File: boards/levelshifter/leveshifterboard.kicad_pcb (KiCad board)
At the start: 2 copper layers, 82.5 x 43.2 mm, 40 parts, among them J1 RJ45, P1 CONN_2, P2 CONN_7, Q1 IRLR110, Q2 NDS355, SW1 SW_PUSH, U1 LM358, U2 SN74LVC1G74, U3 74HCT125, U4 TS2937

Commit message: Fixed levelshifter board
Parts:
- removed Q1: IRLR110, DPAK2
- added D5: ZENER_5.6V, sod123, F.Cu at (158.8, 61.6)
- added D6: ZENER_5.6V, sod123, F.Cu at (148.6, 60.3)
- added D7: ZENER_5.6V, sod123, F.Cu at (144.1, 75.6)
- added D8: ZENER_5.6V, sod123, F.Cu at (146.7, 75.6)
- added R13: 1k, SM0603, F.Cu at (144.8, 63.5)
- added R14: 1k, SM0603, F.Cu at (144.8, 66.0)
- added R15: 1k, SM0603, F.Cu at (144.8, 68.6)
- added R16: 1k, SM0603, F.Cu at (144.8, 71.1)
- added U5: BTS462, TO252-5L, F.Cu at (189.2, 81.3)
- C1: value 100n -> 100nF
- C2, C7: value 100nf -> 100nF
- F1: footprint fuse1 -> fuse22.5
- U2: value SN74LVC1G74 -> 74HC74; footprint SO8E -> SO14E
- moved P1 29.8 mm to (168.3, 48.3)
- moved C7 13.1 mm to (173.4, 62.9), turned to 90 degrees
- moved F1 6.75 mm to (139.7, 51.4)
- moved U2 2.54 mm to (177.2, 67.9), turned to 0 degrees
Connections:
- J1 pad 10: Sense -> (no net)
- R8 pad 1: N-0000024 -> N-0000010
- SW1 pad 1: N-0000024 -> N-0000010
- U2 pad 1: GND -> N-0000010
- U2 pad 3: PowerOn -> GND
- U2 pad 4: GND -> Shutdown
- U2 pad 6: N-0000024 -> PowerOn
- U2 pad 7: Shutdown -> GND
- U2 pad 8: +5V -> (no net)
- U3 pad 11: Reset -> N-0000015
- U3 pad 3: Clock -> N-0000018
- U3 pad 6: Enable -> N-0000017
- U3 pad 8: Data_Out -> N-0000016
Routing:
- net N-0000029: track 7.62 -> 40.4 mm
- net N-0000024: track 26.8 -> 0.00 mm, vias 1 -> 0
- net N-0000010: track 0.00 -> 25.2 mm, vias 0 -> 1
- net N-0000016: track 0.00 -> 15.8 mm, vias 0 -> 3
- net Clock: track 23.8 -> 8.13 mm
- net N-0000018: track 0.00 -> 15.6 mm
- net N-0000015: track 0.00 -> 14.2 mm, vias 0 -> 2
- net N-0000017: track 0.00 -> 13.6 mm, vias 0 -> 2
- net Reset: track 20.5 -> 8.13 mm
- net PowerOn: track 26.2 -> 14.8 mm
- net Data_Out: track 19.1 -> 8.38 mm, vias 3 -> 1
- net Enable: track 18.6 -> 8.13 mm
- net +5V: track 86.6 -> 93.1 mm, vias 5 -> 3
- net Shutdown: track 16.8 -> 18.2 mm
- net N-0000031: track 65.2 -> 64.1 mm

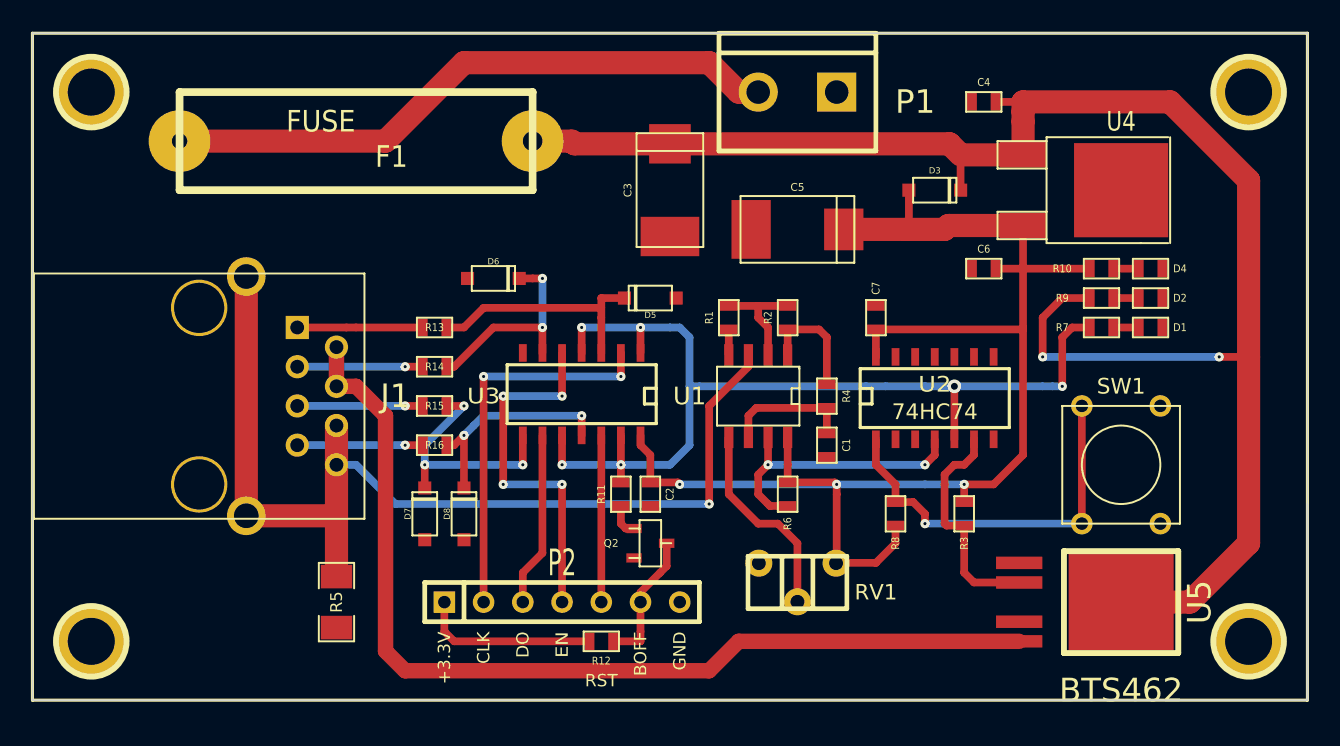
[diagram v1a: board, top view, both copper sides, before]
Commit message: Minor Silkscreen fixes
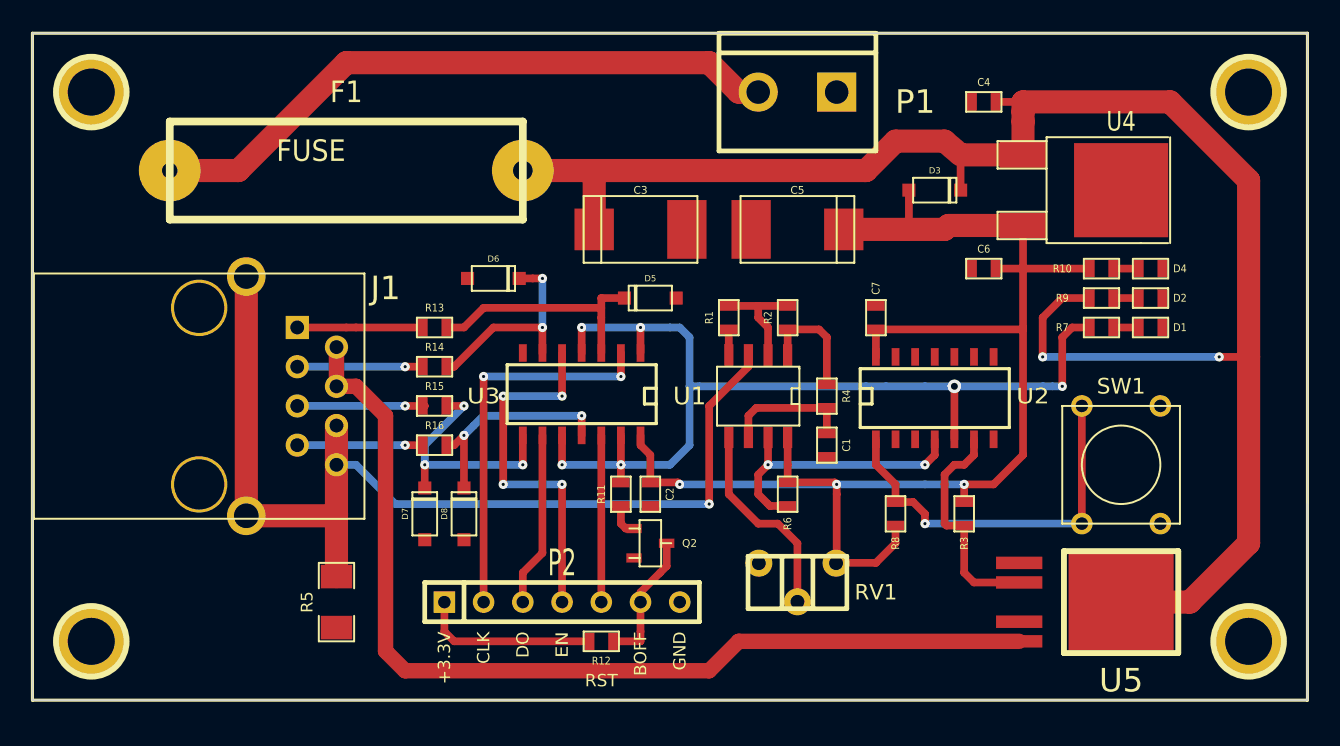
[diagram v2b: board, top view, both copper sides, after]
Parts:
- moved C3 3.18 mm to (158.1, 57.1), turned to 180 degrees
- moved F1 2.01 mm to (139.1, 53.3)
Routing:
- net +24V: track 109.7 -> 114.9 mm
- net N-0000029: track 40.4 -> 41.8 mm
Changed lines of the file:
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@@
     (thickness 1.6)
     (drawings 31)
-    (tracks 260)
+    (tracks 262)
     (zones 0)
     (modules 48)
@@
   (layers
     (15 F.Cu signal)
-    (0 B.Cu signal)
+    (0 B.Cu signal hide)
     (16 B.Adhes user)
     (17 F.Adhes user)
@@
     (descr SOT23)
     (attr smd)
-    (fp_text reference Q2 (at 0 2.54 360) (layer F.SilkS)
+    (fp_text reference Q2 (at 0 -2.54 360) (layer F.SilkS)
       (effects (font (size 0.50038 0.50038) (thickness 0.09906)))
     )
@@
     (at 138.43 81.28 270)
     (attr smd)
-    (fp_text reference R5 (at 0 0 270) (layer F.SilkS)
+    (fp_text reference R5 (at 0 1.905 270) (layer F.SilkS)
       (effects (font (size 0.762 0.762) (thickness 0.127)))
     )
@@
     (at 129.54 67.945 270)
     (tags RJ45)
-    (fp_text reference J1 (at 0 -12.7 360) (layer F.SilkS)
+    (fp_text reference J1 (at -6.985 -12.065 360) (layer F.SilkS)
       (effects (font (size 1.524 1.524) (thickness 0.3048)))
     )
@@
     (at 168.275 57.15)
     (descr "SMT capacitor, tantalum size D")
-    (fp_text reference C5 (at 0 -2.7305) (layer F.SilkS)
+    (fp_text reference C5 (at 0 -2.54) (layer F.SilkS)
       (effects (font (size 0.50038 0.50038) (thickness 0.11938)))
     )
@@
   )
   (module c_tant_D (layer F.Cu)
-    (at 160.02 54.61 90)
+    (at 158.115 57.15 180)
     (descr "SMT capacitor, tantalum size D")
-    (fp_text reference C3 (at 0 -2.7305 90) (layer F.SilkS)
+    (fp_text reference C3 (at 0 2.54 180) (layer F.SilkS)
       (effects (font (size 0.50038 0.50038) (thickness 0.11938)))
     )
-    (fp_text value 10uF (at 0 2.7305 90) (layer F.SilkS) hide
+    (fp_text value 10uF (at 0 2.7305 180) (layer F.SilkS) hide
       (effects (font (size 0.50038 0.50038) (thickness 0.11938)))
     )
@@
     (fp_line (start 3.683 2.159) (end 3.683 -2.159) (layer F.SilkS) (width 0.127))
     (fp_line (start 3.683 -2.159) (end -3.683 -2.159) (layer F.SilkS) (width 0.127))
-    (pad 1 smd rect (at 2.99974 0 90) (size 2.55016 2.70002)
+    (pad 1 smd rect (at 2.99974 0 180) (size 2.55016 2.70002)
       (layers F.Cu F.Paste F.Mask)
       (net 1 +24V)
     )
-    (pad 2 smd rect (at -2.99974 0 90) (size 2.55016 3.79984)
+    (pad 2 smd rect (at -2.99974 0 180) (size 2.55016 3.79984)
       (layers F.Cu F.Paste F.Mask)
       (net 12 GND)
@@
     (at 158.75 61.595 180)
     (descr SOD123)
-    (fp_text reference D5 (at 0 -1.09982 180) (layer F.SilkS)
+    (fp_text reference D5 (at 0 1.27 180) (layer F.SilkS)
       (effects (font (size 0.39878 0.39878) (thickness 0.09906)))
     )
@@
     (at 148.59 60.325)
     (descr SOD123)
-    (fp_text reference D6 (at 0 -1.09982) (layer F.SilkS)
+    (fp_text reference D6 (at 0 -1.27) (layer F.SilkS)
       (effects (font (size 0.39878 0.39878) (thickness 0.09906)))
     )
@@
     (at 144.145 75.565 90)
     (descr SOD123)
-    (fp_text reference D7 (at 0 -1.09982 90) (layer F.SilkS)
+    (fp_text reference D7 (at 0 -1.27 90) (layer F.SilkS)
       (effects (font (size 0.39878 0.39878) (thickness 0.09906)))
     )
@@
     (at 146.685 75.565 90)
     (descr SOD123)
-    (fp_text reference D8 (at 0 -1.09982 90) (layer F.SilkS)
+    (fp_text reference D8 (at 0 -1.27 90) (layer F.SilkS)
       (effects (font (size 0.39878 0.39878) (thickness 0.09906)))
     )
@@
     (at 144.78 63.5 180)
     (attr smd)
-    (fp_text reference R13 (at 0 0 180) (layer F.SilkS)
+    (fp_text reference R13 (at 0 1.27 180) (layer F.SilkS)
       (effects (font (size 0.508 0.4572) (thickness 0.1143)))
     )
@@
     (at 144.78 66.04 180)
     (attr smd)
-    (fp_text reference R14 (at 0 0 180) (layer F.SilkS)
+    (fp_text reference R14 (at 0 1.27 180) (layer F.SilkS)
       (effects (font (size 0.508 0.4572) (thickness 0.1143)))
     )
@@
     (at 144.78 68.58 180)
     (attr smd)
-    (fp_text reference R15 (at 0 0 180) (layer F.SilkS)
+    (fp_text reference R15 (at 0 1.27 180) (layer F.SilkS)
       (effects (font (size 0.508 0.4572) (thickness 0.1143)))
     )
@@
     (at 144.78 71.12 180)
     (attr smd)
-    (fp_text reference R16 (at 0 0 180) (layer F.SilkS)
+    (fp_text reference R16 (at 0 1.27 180) (layer F.SilkS)
       (effects (font (size 0.508 0.4572) (thickness 0.1143)))
     )
@@
     (tags "CMS SOJ")
     (attr smd)
-    (fp_text reference U2 (at 0 -0.762) (layer F.SilkS)
+    (fp_text reference U2 (at 6.35 0) (layer F.SilkS)
       (effects (font (size 1.016 1.143) (thickness 0.127)))
     )
-    (fp_text value 74HC74 (at 0 1.016) (layer F.SilkS)
+    (fp_text value 74HC74 (at 0 1.016) (layer F.SilkS) hide
       (effects (font (size 1.016 1.016) (thickness 0.127)))
     )
@@
   (module TO252-5L (layer F.Cu)
     (at 189.23 81.28 270)
-    (fp_text reference U5 (at 0 -5.08 270) (layer F.SilkS)
+    (fp_text reference U5 (at 5.08 0 360) (layer F.SilkS)
       (effects (font (size 1.524 1.524) (thickness 0.3048)))
     )
-    (fp_text value BTS462 (at 5.715 0 360) (layer F.SilkS)
+    (fp_text value BTS462 (at 5.08 0 360) (layer F.SilkS) hide
       (effects (font (size 1.524 1.524) (thickness 0.3048)))
     )
@@
   )
   (module fuse22.5 (layer F.Cu)
-    (at 139.7 51.435)
+    (at 139.065 53.34)
     (descr "Resitance 7 pas")
     (tags R)
     (autoplace_cost180 10)
-    (fp_text reference F1 (at 2.286 1.016) (layer F.SilkS)
+    (fp_text reference F1 (at 0 -5.08) (layer F.SilkS)
       (effects (font (size 1.397 1.27) (thickness 0.2032)))
     )
@@
     (arrow2b (pts (xy 102.87 40.005001) (xy 103.996503 39.418581)))
   )
-  (segment (start 160.02 51.61026) (end 153.84526 51.61026) (width 1.5) (layer F.Cu) (net 1))
-  (segment (start 153.67 51.435) (end 151.13 51.435) (width 1.5) (layer F.Cu) (net 1))
-  (segment (start 153.84526 51.61026) (end 153.67 51.435) (width 1.5) (layer F.Cu) (net 1))
+  (segment (start 155.11526 57.15) (end 155.11526 53.34) (width 1.5) (layer F.Cu) (net 1) (status 400000))
+  (segment (start 172.72 53.34) (end 155.575 53.34) (width 1.5) (layer F.Cu) (net 1))
+  (segment (start 155.575 53.34) (end 151.13 53.34) (width 1.5) (layer F.Cu) (net 1))
+  (segment (start 174.625 51.435) (end 172.72 53.34) (width 1.5) (layer F.Cu) (net 1))
+  (segment (start 178.83886 52.324) (end 177.8 51.435) (width 1.5) (layer F.Cu) (net 1))
+  (segment (start 177.8 51.435) (end 174.625 51.435) (width 1.5) (layer F.Cu) (net 1))
+  (segment (start 151.13 53.34) (end 150.495 53.34) (width 1.5) (layer F.Cu) (net 1) (status 800020))
   (segment (start 181.102 48.895) (end 182.88 48.895) (width 0.5) (layer F.Cu) (net 1))
   (via (at 184.15 65.405) (size 0.6) (drill 0.2) (layers F.Cu B.Cu) (net 1))
@@
   (segment (start 182.88 50.165) (end 182.88 52.324) (width 1.5) (layer F.Cu) (net 1))
   (segment (start 192.405 48.895) (end 182.88 48.895) (width 1.5) (layer F.Cu) (net 1))
-  (segment (start 178.83886 52.324) (end 178.12512 51.61026) (width 1.5) (layer F.Cu) (net 1))
-  (segment (start 178.12512 51.61026) (end 160.02 51.61026) (width 1.5) (layer F.Cu) (net 1))
   (segment (start 178.83886 54.61) (end 178.83886 52.324) (width 0.5) (layer F.Cu) (net 1))
   (segment (start 179.07 52.705) (end 179.07 52.324) (width 0.5) (layer F.Cu) (net 1))
@@
   (segment (start 169.672 63.627) (end 170.18 64.135) (width 0.5) (layer F.Cu) (net 21))
   (segment (start 167.64 65.278) (end 167.64 63.627) (width 0.5) (layer F.Cu) (net 21))
-  (segment (start 128.27 51.435) (end 141.605 51.435) (width 1.5) (layer F.Cu) (net 22))
+  (segment (start 127.635 53.34) (end 132.08 53.34) (width 1.5) (layer F.Cu) (net 22) (status 400010))
   (segment (start 164.465 48.26) (end 165.735 48.26) (width 1.5) (layer F.Cu) (net 22) (status 20))
   (segment (start 162.56 46.355) (end 164.465 48.26) (width 1.5) (layer F.Cu) (net 22))
-  (segment (start 146.685 46.355) (end 162.56 46.355) (width 1.5) (layer F.Cu) (net 22))
-  (segment (start 141.605 51.435) (end 146.685 46.355) (width 1.5) (layer F.Cu) (net 22))
+  (segment (start 139.065 46.355) (end 162.56 46.355) (width 1.5) (layer F.Cu) (net 22))
+  (segment (start 132.08 53.34) (end 139.065 46.355) (width 1.5) (layer F.Cu) (net 22))
   (segment (start 188.722 59.69) (end 190.373 59.69) (width 0.5) (layer F.Cu) (net 23) (status 10))
   (segment (start 138.43 67.31) (end 138.43 64.77) (width 1) (layer F.Cu) (net 24))

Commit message: Final fixes to board layouts
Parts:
- moved P1 5.08 mm to (163.2, 48.3)
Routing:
- net N-0000029: track 41.8 -> 35.1 mm
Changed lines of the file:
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@@
     (links 97)
     (no_connects 0)
-    (area 83.440001 10.1575 233.0475 88.1634)
+    (area 83.440001 10.1575 233.0475 87.730001)
     (thickness 1.6)
     (drawings 31)
@@
   (layers
     (15 F.Cu signal)
-    (0 B.Cu signal hide)
+    (0 B.Cu signal)
     (16 B.Adhes user)
     (17 F.Adhes user)
     (18 B.Paste user)
     (19 F.Paste user)
-    (20 B.SilkS user hide)
+    (20 B.SilkS user)
     (21 F.SilkS user)
     (22 B.Mask user)
@@
   )
   (setup
-    (last_trace_width 1.5)
+    (last_trace_width 0.254)
     (user_trace_width 0.3)
     (user_trace_width 0.5)
@@
     (visible_elements FFFFFFBF)
     (pcbplotparams
-      (layerselection 272400385)
+      (layerselection 284983297)
       (usegerberextensions true)
       (excludeedgelayer true)
@@
       (plotinvisibletext false)
       (padsonsilk false)
-      (subtractmaskfromsilk true)
+      (subtractmaskfromsilk false)
       (outputformat 1)
       (mirror false)
@@
   )
   (module bornier2 (layer F.Cu)
-    (at 168.275 48.26 180)
+    (at 163.195 48.26 180)
     (descr "Bornier d'alimentation 2 pins")
     (tags DEV)
@@
     (arrow2b (pts (xy 102.87 40.005001) (xy 103.996503 39.418581)))
   )
-  (segment (start 155.11526 57.15) (end 155.11526 53.34) (width 1.5) (layer F.Cu) (net 1) (status 400000))
+  (segment (start 155.11526 57.15) (end 155.11526 53.34) (width 1.5) (layer F.Cu) (net 1))
   (segment (start 172.72 53.34) (end 155.575 53.34) (width 1.5) (layer F.Cu) (net 1))
   (segment (start 155.575 53.34) (end 151.13 53.34) (width 1.5) (layer F.Cu) (net 1))
@@
   (segment (start 178.83886 52.324) (end 177.8 51.435) (width 1.5) (layer F.Cu) (net 1))
   (segment (start 177.8 51.435) (end 174.625 51.435) (width 1.5) (layer F.Cu) (net 1))
-  (segment (start 151.13 53.34) (end 150.495 53.34) (width 1.5) (layer F.Cu) (net 1) (status 800020))
+  (segment (start 151.13 53.34) (end 150.495 53.34) (width 1.5) (layer F.Cu) (net 1) (status 20))
   (segment (start 181.102 48.895) (end 182.88 48.895) (width 0.5) (layer F.Cu) (net 1))
   (via (at 184.15 65.405) (size 0.6) (drill 0.2) (layers F.Cu B.Cu) (net 1))
@@
   (segment (start 169.672 63.627) (end 170.18 64.135) (width 0.5) (layer F.Cu) (net 21))
   (segment (start 167.64 65.278) (end 167.64 63.627) (width 0.5) (layer F.Cu) (net 21))
-  (segment (start 127.635 53.34) (end 132.08 53.34) (width 1.5) (layer F.Cu) (net 22) (status 400010))
-  (segment (start 164.465 48.26) (end 165.735 48.26) (width 1.5) (layer F.Cu) (net 22) (status 20))
-  (segment (start 162.56 46.355) (end 164.465 48.26) (width 1.5) (layer F.Cu) (net 22))
-  (segment (start 139.065 46.355) (end 162.56 46.355) (width 1.5) (layer F.Cu) (net 22))
-  (segment (start 132.08 53.34) (end 139.065 46.355) (width 1.5) (layer F.Cu) (net 22))
+  (segment (start 137.16 48.26) (end 158.115 48.26) (width 1.5) (layer F.Cu) (net 22))
+  (segment (start 132.08 53.34) (end 137.16 48.26) (width 1.5) (layer F.Cu) (net 22))
+  (segment (start 127.635 53.34) (end 132.08 53.34) (width 1.5) (layer F.Cu) (net 22) (status 10))
+  (segment (start 158.115 48.26) (end 160.655 48.26) (width 1.5) (layer F.Cu) (net 22))
+  (segment (start 158.115 48.26) (end 158.115 48.26) (width 1.5) (layer F.Cu) (net 22))
   (segment (start 188.722 59.69) (end 190.373 59.69) (width 0.5) (layer F.Cu) (net 23) (status 10))
   (segment (start 138.43 67.31) (end 138.43 64.77) (width 1) (layer F.Cu) (net 24))

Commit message: Updated version number
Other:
- board text added: "Version 1.1"
- board text removed: "Version 1.0"
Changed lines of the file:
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@@
     (pcbplotparams
       (layerselection 284983297)
-      (usegerberextensions true)
+      (usegerberextensions false)
       (excludeedgelayer true)
       (linewidth 0.150000)
@@
       (padsonsilk false)
       (subtractmaskfromsilk false)
-      (outputformat 1)
+      (outputformat 2)
       (mirror false)
-      (drillshape 0)
+      (drillshape 2)
       (scaleselection 1)
-      (outputdirectory gerber/))
+      (outputdirectory plot))
   )
   (net 0 "")
@@
     (effects (font (size 1.5 1.5) (thickness 0.3)) (justify mirror))
   )
-  (gr_text "Version 1.0" (at 191.135 66.04) (layer B.SilkS)
+  (gr_text "Version 1.1" (at 191.135 66.04) (layer B.SilkS)
     (effects (font (size 1.5 1.5) (thickness 0.3)) (justify left mirror))
   )

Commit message: Added logos
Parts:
- added G***: logo_hacker_silkbot_10_00mm, logo_hacker_silkbot_10_00mm, B.Cu at (138.4, 80.6)
